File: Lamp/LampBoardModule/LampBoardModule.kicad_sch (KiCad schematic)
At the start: 87 parts, among them IC1 L7805ABD2T-TR, IC2 SN74LVC2T45DCUR, J1 DS1023-1x3SF11, J2 DS1023-1x3SF11, J3 284514-3, J4 DC-005-A250, Q1 CMN3406M, SW1 PEC11R, SW2 MT-0-102, U1 RP2040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

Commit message: Final version ready to roll
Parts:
- removed D12: D_Schottky, Diode_SMD:D_SMA, symbol Device:D_Schottky
- removed D13: GREEN, LED_SMD:LED_0603_1608Metric, symbol Device:LED
- removed J2: DS1023-1x3SF11, easyeda2kicad:HDR-TH_3P-P2.54-V-F-1, symbol easyeda2kicad:DS1023-1X3SF11
- removed R24, R25: 2.4k, Resistor_SMD:R_0805_2012Metric, symbol Device:R_Small_US
- removed R26, R27: 330, Resistor_SMD:R_0603_1608Metric, symbol Device:R_Small_US
- removed U3, U4: LTV357T-B, easyeda2kicad:SOP-4_L4.4-W4.0-P2.54-LS7.0-TL, symbol easyeda2kicad:LTV357T-B
- added Q2: FH38P03G6, easyeda2kicad:DFN-8_L3.3-W3.3-P0.65-BL-EP, symbol easyeda2kicad:FH38P03G6
- C8: LCSC C15195 -> C92487; LCSC Part C15195 -> C92487
- CR1: footprint LD1117S33CTR:SOT-223_STM -> easyeda2kicad:SOT-223-4_L6.5-W3.5-P2.30-LS7.0-BR; symbol LD1117S33CTR:LD1117S33CTR -> easyeda2kicad:LD1117S33CTR
- R17: value 330 -> 10k; LCSC C23138 -> C15401; LCSC Part C23138 -> C15401
- R19: value 100 -> 10k; LCSC C22775 -> C15401; LCSC Part C22775 -> C15401
- R20: value 1K -> 10k; footprint Resistor_SMD:R_0402_1005Metric -> Resistor_SMD:R_0603_1608Metric; LCSC C25543 -> C15401; LCSC Part C25543 -> C15401
- R21, R22, R23, R7: value 10K -> 10k
- SW1: LCSC (none) -> C7435302; LCSC Part (none) -> C7435302
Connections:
- net P_SEN is gone; now on net +24V: SW2.1
- net +24V: now also R19.2, Q2.1 (S), Q2.2 (S), Q2.3 (S); no longer C4.1, J3.1, SW2.3
- net +3.3V: now also CR1.4 (VOUT)
- net GND: now also J3.3, R17.1; no longer R17.2, R20.2
- net LED_D: now also U1.15 (GPIO12); no longer U1.28 (GPIO17)
- net LED_EN: now also Q1.1 (G), R17.2, U1.28 (GPIO17); no longer U1.15 (GPIO12)
- net at Q1.3 (D): now also R20.1; no longer J3.3
- net P_SEN_LED: no longer names the net of U1.37 (GPIO25)
- net P_SEN_O: no longer names the net of U1.38 (GPIO26_ADC0)
- new net: Q2.4 (G), R19.1, R20.2
- new net: C4.1, J3.1, Q2.5 (D), Q2.6 (D), Q2.7 (D), Q2.8 (D)
- no-connect marks 19 -> 22
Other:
- note removed: "Party"
- moved on the sheet: C4, C7, C8, D1, D2, D3, D4, D9, J1, J3, R16, R2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

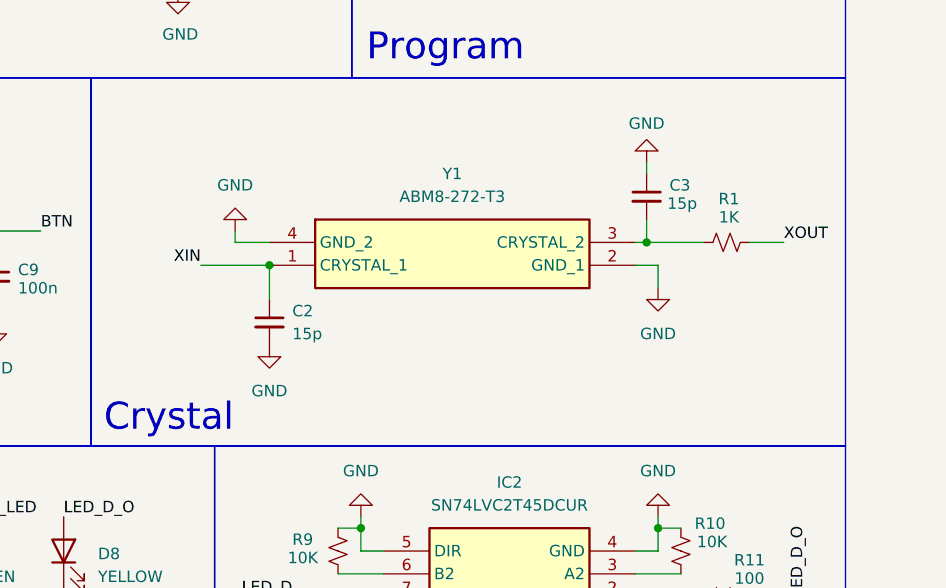
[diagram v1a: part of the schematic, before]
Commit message: Finished lamp saving; cad v0.4
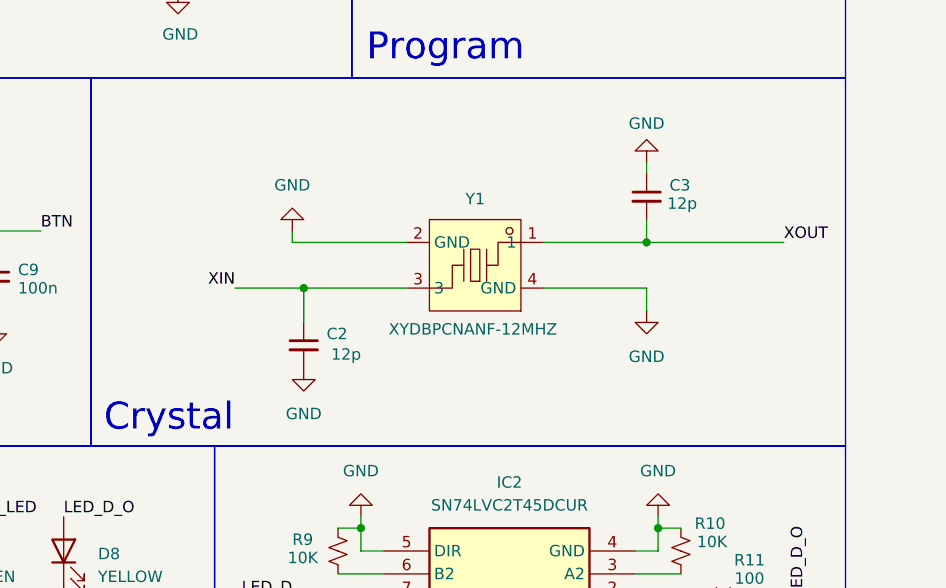
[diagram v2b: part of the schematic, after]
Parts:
- removed R1: 1K, Resistor_SMD:R_0402_1005Metric, symbol Device:R_Small_US
- C2, C3: value 15p -> 12p; LCSC C86285 -> C1547; LCSC Part C86285 -> C1547
- Y1: value ABM8-272-T3 -> XYDBPCNANF-12MHZ; footprint ABM8-272-T3:ABM8272T3 -> easyeda2kicad:OSC-SMD_4P-L2.5-W2.0-BL; symbol ABM8-272-T3:ABM8-272-T3 -> easyeda2kicad:XYDBPCNANF-12MHZ; LCSC C20625731 -> C521567; LCSC Part C20625731 -> C521567
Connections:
- net XIN: now also Y1.3; no longer Y1.1 (CRYSTAL_1)
- net XOUT: now also C3.2, Y1.1
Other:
- moved on the sheet: C2
